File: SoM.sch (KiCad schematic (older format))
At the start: 19 parts, among them J7 MC-HVT1-S04-G, U10 SA800U-WF

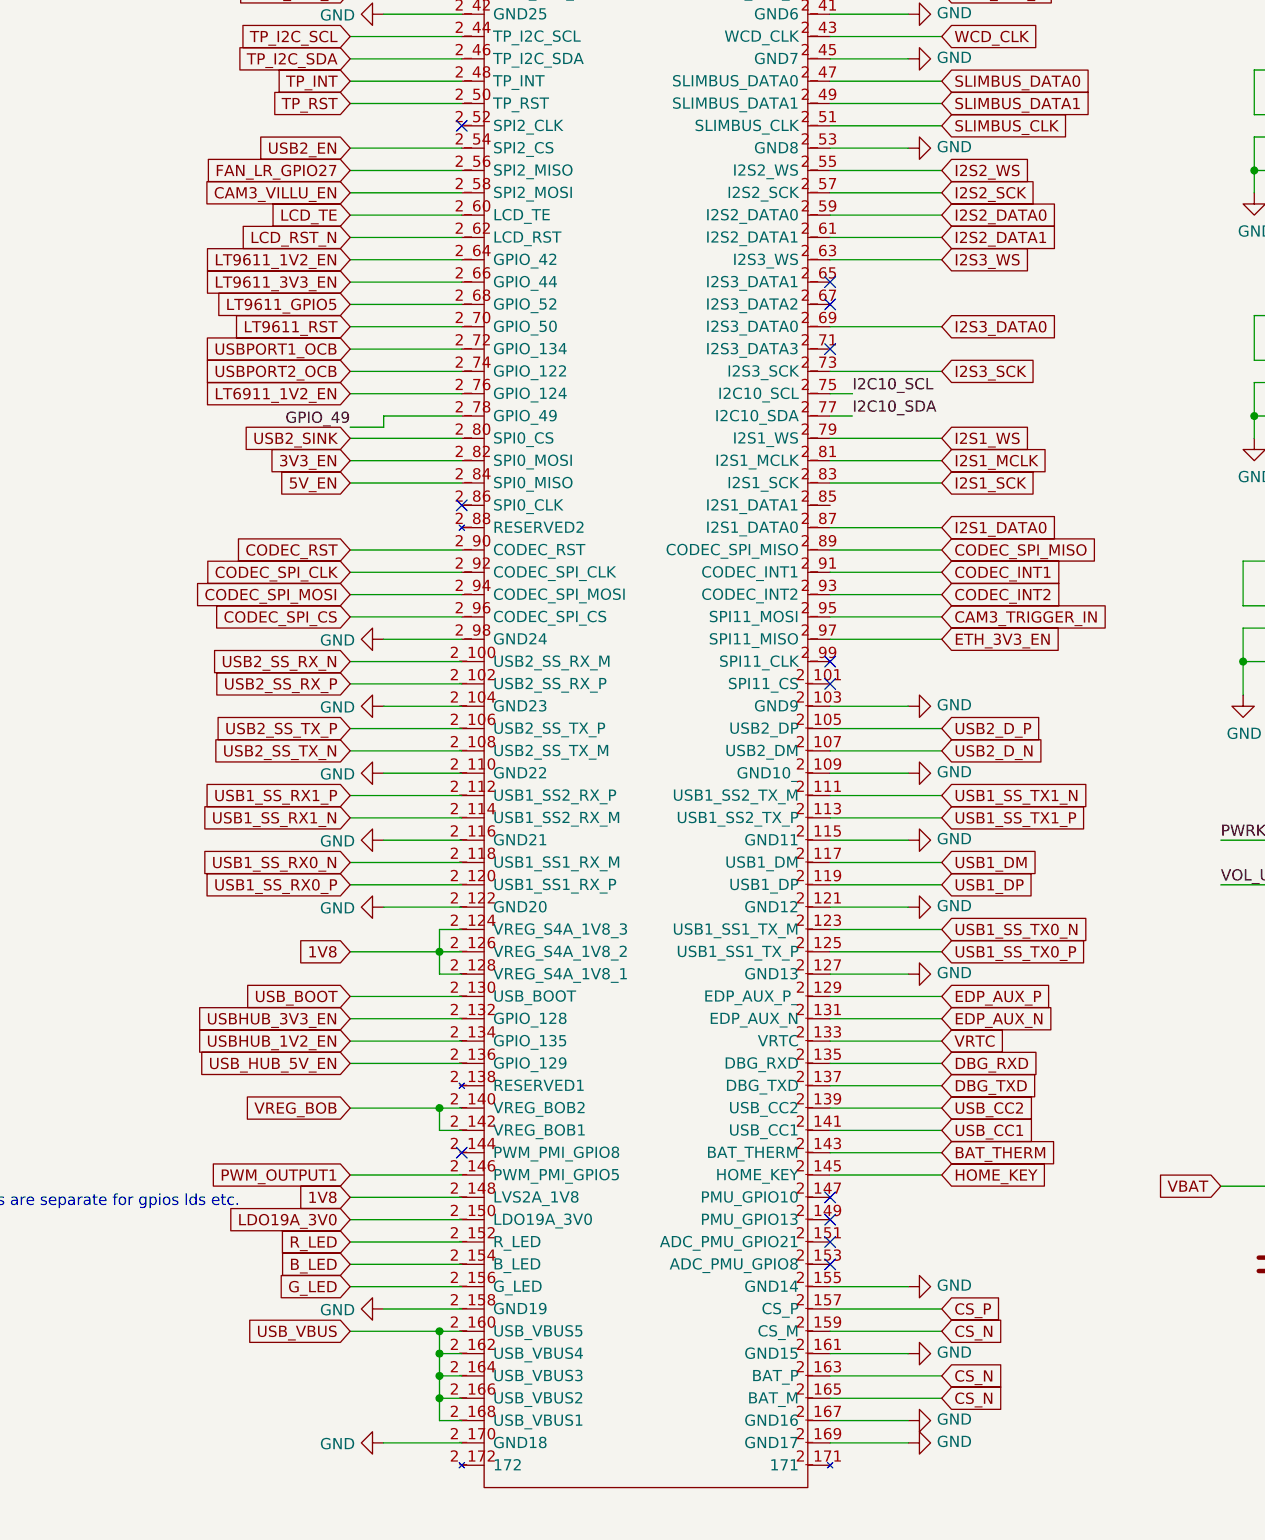
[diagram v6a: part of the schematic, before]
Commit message: fixing ERC errors
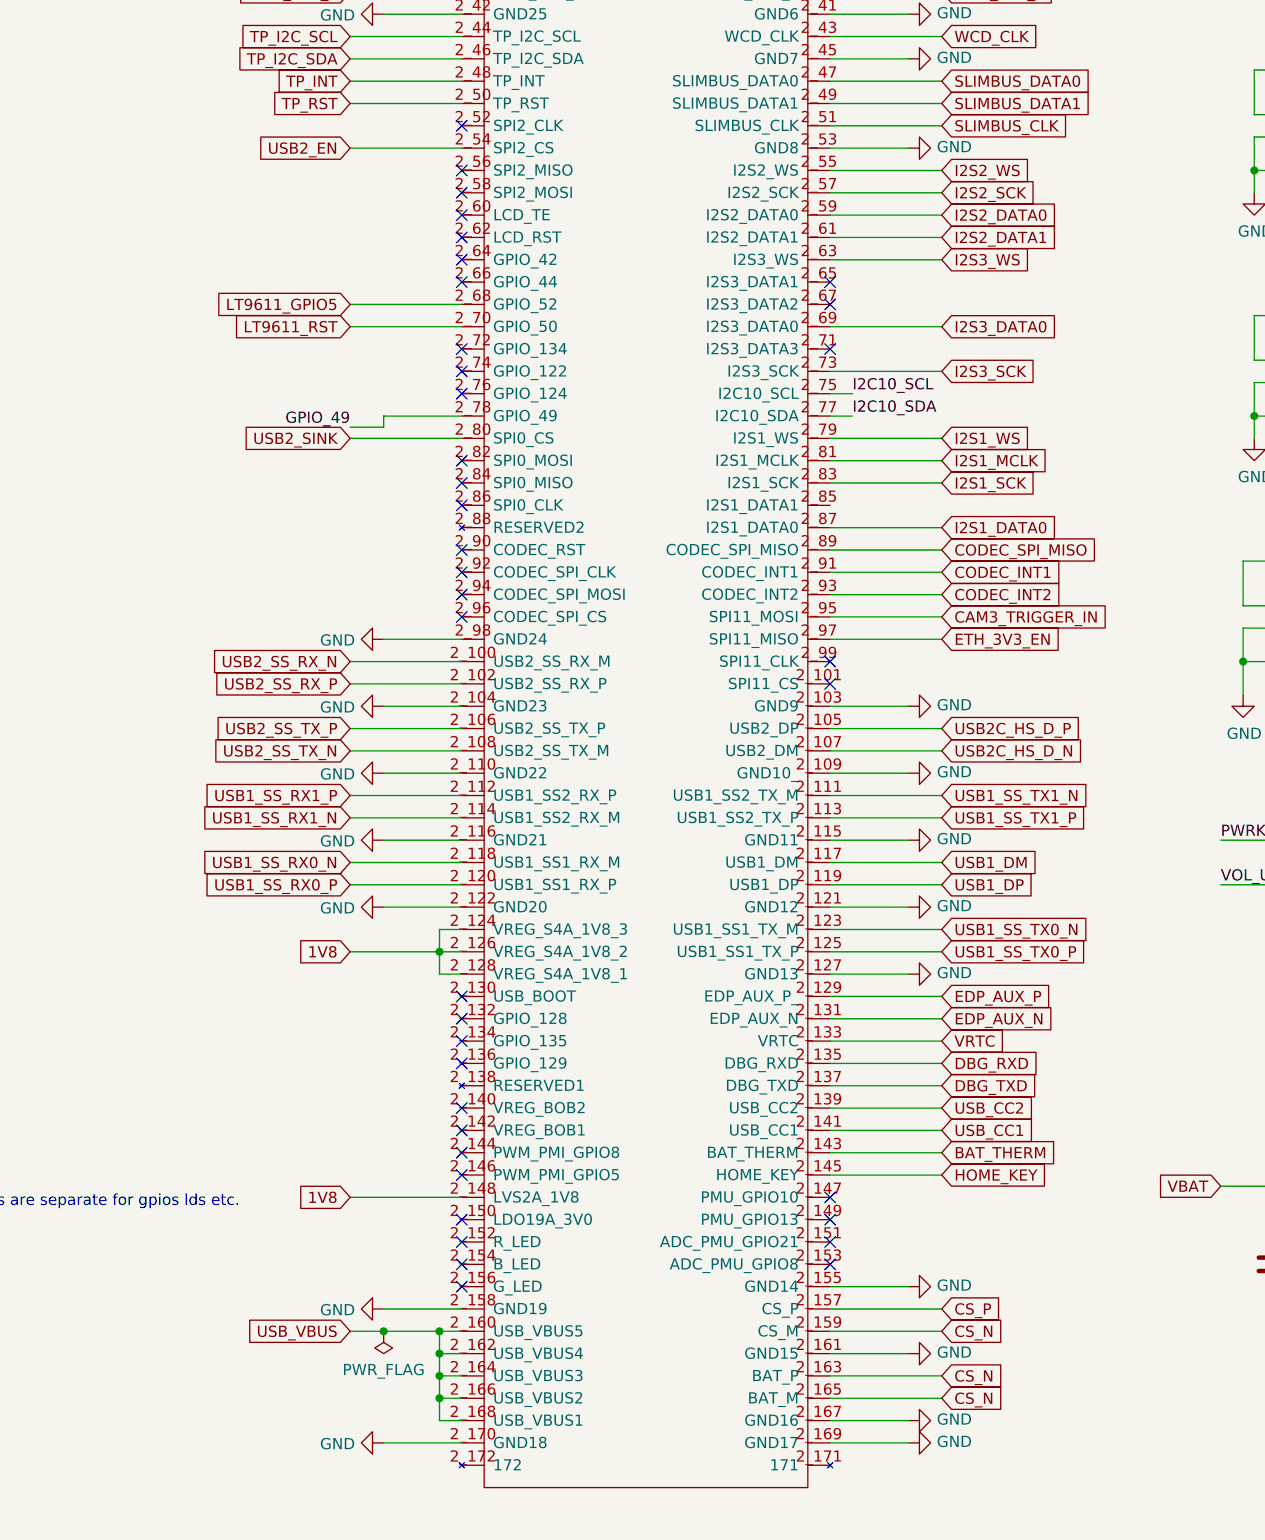
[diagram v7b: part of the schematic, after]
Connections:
- net 3V3_EN: no longer names the net of U10.2_82 (SPI0_MOSI)
- net 5V_EN: no longer names the net of U10.2_84 (SPI0_MISO)
- net B_LED: no longer names the net of U10.2_154 (B_LED)
- net CAM3_VILLU_EN: no longer names the net of U10.2_58 (SPI2_MOSI)
- net CODEC_RST: no longer names the net of U10.2_90 (CODEC_RST)
- net CODEC_SPI_CLK: no longer names the net of U10.2_92 (CODEC_SPI_CLK)
- net CODEC_SPI_CS: no longer names the net of U10.2_96 (CODEC_SPI_CS)
- net CODEC_SPI_MOSI: no longer names the net of U10.2_94 (CODEC_SPI_MOSI)
- net FAN_LR_GPIO27: no longer names the net of U10.2_56 (SPI2_MISO)
- net G_LED: no longer names the net of U10.2_156 (G_LED)
- net LCD_RST_N: no longer names the net of U10.2_62 (LCD_RST)
- net LCD_TE: no longer names the net of U10.2_60 (LCD_TE)
- net LDO19A_3V0: no longer names the net of U10.2_150 (LDO19A_3V0)
- net LT6911_1V2_EN: no longer names the net of U10.2_76 (GPIO_124)
- net LT9611_1V2_EN: no longer names the net of U10.2_64 (GPIO_42)
- net LT9611_3V3_EN: no longer names the net of U10.2_66 (GPIO_44)
- net PWM_OUTPUT1: no longer names the net of U10.2_146 (PWM_PMI_GPIO5)
- net R_LED: no longer names the net of U10.2_152 (R_LED)
- net USB2_D_N renamed USB2C_HS_D_N
- net USB2_D_P renamed USB2C_HS_D_P
- net USBHUB_1V2_EN: no longer names the net of U10.2_134 (GPIO_135)
- net USBHUB_3V3_EN: no longer names the net of U10.2_132 (GPIO_128)
- net USBPORT1_OCB: no longer names the net of U10.2_72 (GPIO_134)
- net USBPORT2_OCB: no longer names the net of U10.2_74 (GPIO_122)
- net USB_BOOT: no longer names the net of U10.2_130 (USB_BOOT)
- net USB_HUB_5V_EN: no longer names the net of U10.2_136 (GPIO_129)
- net VREG_BOB: no longer names the net of U10.2_140 (VREG_BOB2)
- net VREG_BOB: no longer U10.2_142 (VREG_BOB1)
- no-connect marks 35 -> 61
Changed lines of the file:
@@
-$EndComp
-$Comp
-L sa800u-baseboard-hw:GND #PWR0118
-U 1 1 61F4308E
-P 7750 9300
-F 0 "#PWR0118" H 7750 9050 50  0001 C CNN
-F 1 "GND" V 7755 9172 50  0000 R CNN
-F 2 "" H 7750 9300 50  0001 C CNN
-F 3 "" H 7750 9300 50  0001 C CNN
-	1    7750 9300
-	0    1    1    0
 $EndComp
 $Comp
@@
 TP_RST
 NoConn ~ 8100 4000
-Text GLabel 7600 4200 0    50   Input ~ 0
-FAN_LR_GPIO27
-Text GLabel 7600 4300 0    50   Input ~ 0
-CAM3_VILLU_EN
-Text GLabel 7600 4400 0    50   Input ~ 0
-LCD_TE
-Text GLabel 7600 4500 0    50   Input ~ 0
-LCD_RST_N
-Text GLabel 7600 4600 0    50   Input ~ 0
-LT9611_1V2_EN
-Text GLabel 7600 4700 0    50   Input ~ 0
-LT9611_3V3_EN
 Text GLabel 7600 4800 0    50   Input ~ 0
 LT9611_GPIO5
 Text GLabel 7600 4900 0    50   Input ~ 0
 LT9611_RST
-Text GLabel 7600 5000 0    50   Input ~ 0
-USBPORT1_OCB
-Text GLabel 7600 5100 0    50   Input ~ 0
-USBPORT2_OCB
-Text GLabel 7600 5200 0    50   Input ~ 0
-LT6911_1V2_EN
-Text GLabel 7600 5500 0    50   Input ~ 0
-3V3_EN
-Text GLabel 7600 5600 0    50   Input ~ 0
-5V_EN
 NoConn ~ 8100 5700
-Text GLabel 7600 5900 0    50   Input ~ 0
-CODEC_RST
-Text GLabel 7600 6000 0    50   Input ~ 0
-CODEC_SPI_CLK
-Text GLabel 7600 6100 0    50   Input ~ 0
-CODEC_SPI_MOSI
-Text GLabel 7600 6200 0    50   Input ~ 0
-CODEC_SPI_CS
 Text GLabel 7600 6400 0    50   Input ~ 0
 USB2_SS_RX_N
@@
 Wire Wire Line
 	8000 7800 8100 7800
-Text GLabel 7600 7900 0    50   Input ~ 0
-USB_BOOT
-Text GLabel 7600 8000 0    50   Input ~ 0
-USBHUB_3V3_EN
-Text GLabel 7600 8100 0    50   Input ~ 0
-USBHUB_1V2_EN
-Text GLabel 7600 8200 0    50   Input ~ 0
-USB_HUB_5V_EN
-Text GLabel 7600 8400 0    50   Input ~ 0
-VREG_BOB
-Wire Wire Line
-	7600 8400 8000 8400
-Wire Wire Line
-	8000 8400 8000 8500
-Wire Wire Line
-	8000 8500 8100 8500
-Connection ~ 8000 8400
-Wire Wire Line
-	8000 8400 8100 8400
 NoConn ~ 8100 8600
-Text GLabel 7600 8700 0    50   Input ~ 0
-PWM_OUTPUT1
 Text GLabel 7600 8800 0    50   Input ~ 0
 1V8
 Text Notes 5050 8850 0    50   ~ 0
 In reference design this 1V8s are separate for gpios lds etc.\n
-Text GLabel 7600 8900 0    50   Input ~ 0
-LDO19A_3V0
-Text GLabel 7600 9000 0    50   Input ~ 0
-R_LED
-Text GLabel 7600 9100 0    50   Input ~ 0
-B_LED
-Text GLabel 7600 9200 0    50   Input ~ 0
-G_LED
 Text GLabel 7600 9400 0    50   Input ~ 0
 USB_VBUS
 Wire Wire Line
-	7600 9400 8000 9400
+	7600 9400 7750 9400
 Wire Wire Line
 	8000 9400 8000 9500
@@
 	8000 9500 8000 9600
 Wire Wire Line
-	7600 9200 8100 9200
-Wire Wire Line
-	7600 9100 8100 9100
-Wire Wire Line
-	8100 9000 7600 9000
-Wire Wire Line
-	7600 8900 8100 8900
-Wire Wire Line
 	8100 8800 7600 8800
 Wire Wire Line
-	7600 8700 8100 8700
-Wire Wire Line
-	8100 8200 7600 8200
-Wire Wire Line
-	7600 8100 8100 8100
-Wire Wire Line
-	8100 8000 7600 8000
-Wire Wire Line
-	7600 7900 8100 7900
-Wire Wire Line
 	8100 7400 7600 7400
 Wire Wire Line
@@
 	7600 6400 8100 6400
 Wire Wire Line
-	8100 6200 7600 6200
-Wire Wire Line
-	7600 6100 8100 6100
-Wire Wire Line
-	8100 6000 7600 6000
-Wire Wire Line
-	7600 5900 8100 5900
-Wire Wire Line
-	8100 5600 7600 5600
-Wire Wire Line
-	7600 5500 8100 5500
-Wire Wire Line
-	7600 5200 8100 5200
-Wire Wire Line
-	8100 5100 7600 5100
-Wire Wire Line
-	7600 5000 8100 5000
-Wire Wire Line
 	8100 4900 7600 4900
 Wire Wire Line
 	7600 4800 8100 4800
-Wire Wire Line
-	8100 4700 7600 4700
-Wire Wire Line
-	7600 4600 8100 4600
-Wire Wire Line
-	8100 4500 7600 4500
-Wire Wire Line
-	7600 4400 8100 4400
-Wire Wire Line
-	8100 4300 7600 4300
-Wire Wire Line
-	7600 4200 8100 4200
 Wire Wire Line
 	7600 3900 8100 3900
@@
 NoConn ~ 9750 6500
 Text GLabel 10250 6700 2    50   Input ~ 0
-USB2_D_P
+USB2C_HS_D_P
 Text GLabel 10250 6800 2    50   Input ~ 0
-USB2_D_N
+USB2C_HS_D_N
 Wire Wire Line
 	9750 6900 10100 6900
@@
 Wire Wire Line
 	12150 9350 11750 9350
+NoConn ~ 8100 8400
+NoConn ~ 8100 8500
+NoConn ~ 8100 7900
+NoConn ~ 8100 8000
+NoConn ~ 8100 8100
+NoConn ~ 8100 8200
+NoConn ~ 8100 5900
+NoConn ~ 8100 6000
+NoConn ~ 8100 6100
+NoConn ~ 8100 6200
+NoConn ~ 8100 8700
+NoConn ~ 8100 5500
+NoConn ~ 8100 5600
+$Comp
+L sa800u-baseboard-hw:GND #PWR0118
+U 1 1 62A6F314
+P 7750 9300
+F 0 "#PWR0118" H 7750 9050 50  0001 C CNN
+F 1 "GND" V 7755 9172 50  0000 R CNN
+F 2 "" H 7750 9300 50  0001 C CNN
+F 3 "" H 7750 9300 50  0001 C CNN
+	1    7750 9300
+	0    1    1    0
+$EndComp
+$Comp
+L power:PWR_FLAG #FLG0118
+U 1 1 62A98DBC
+P 7750 9400
+F 0 "#FLG0118" H 7750 9475 50  0001 C CNN
+F 1 "PWR_FLAG" H 7750 9573 50  0000 C CNN
+F 2 "" H 7750 9400 50  0001 C CNN
+F 3 "~" H 7750 9400 50  0001 C CNN
+	1    7750 9400
+	-1   0    0    1
+$EndComp
+Connection ~ 7750 9400
+Wire Wire Line
+	7750 9400 8000 9400
+NoConn ~ 8100 8900
+NoConn ~ 8100 9000
+NoConn ~ 8100 9100
+NoConn ~ 8100 9200
+NoConn ~ 8100 4200
+NoConn ~ 8100 4300
+NoConn ~ 8100 4400
+NoConn ~ 8100 4500
+NoConn ~ 8100 4600
+NoConn ~ 8100 4700
+NoConn ~ 8100 5000
+NoConn ~ 8100 5100
+NoConn ~ 8100 5200
 $EndSCHEMATC

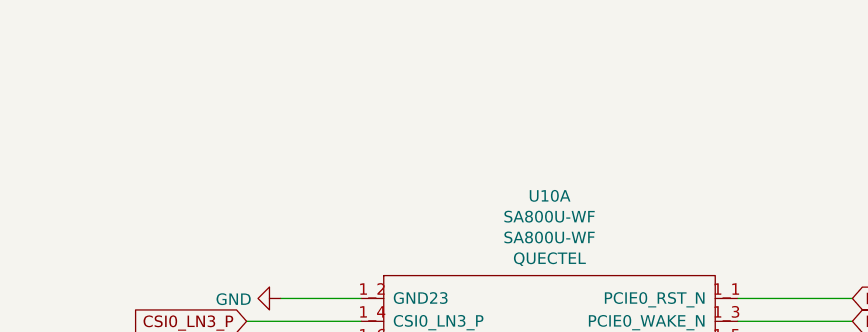
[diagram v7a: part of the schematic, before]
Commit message: Add comment on 3D models
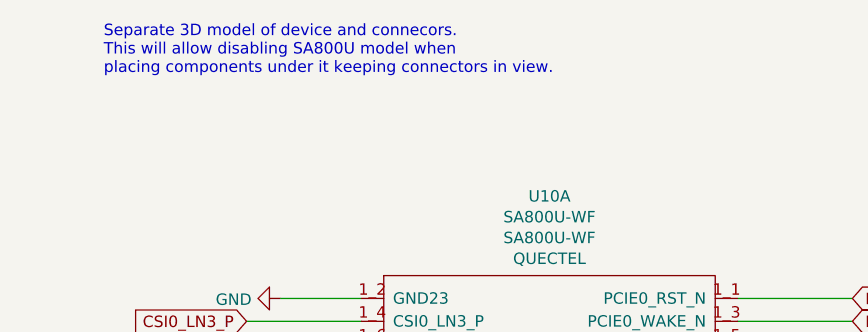
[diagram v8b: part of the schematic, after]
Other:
- note added: "Separate 3D model of device and connecors.\nThis will allow disabling SA800U model when \nplacing components under it keeping connectors in view."
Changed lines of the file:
@@
 NoConn ~ 8100 5100
 NoConn ~ 8100 5200
+Text Notes 525  775  0    50   ~ 0
+Separate 3D model of device and connecors.\nThis will allow disabling SA800U model when \nplacing components under it keeping connectors in view.
 $EndSCHEMATC
